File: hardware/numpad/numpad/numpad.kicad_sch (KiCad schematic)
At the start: 33 parts, among them IC1 LD1117-3.3V-SOT223, J1 Conn_01x06, SW2 Push_Button, Y1 8MHz

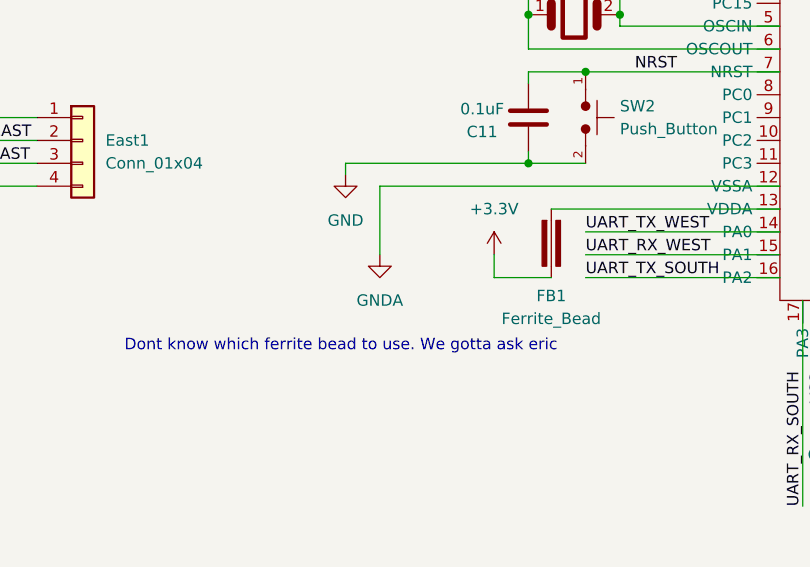
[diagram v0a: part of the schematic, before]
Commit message: typo in schematic
i changed the GNDA to AGND
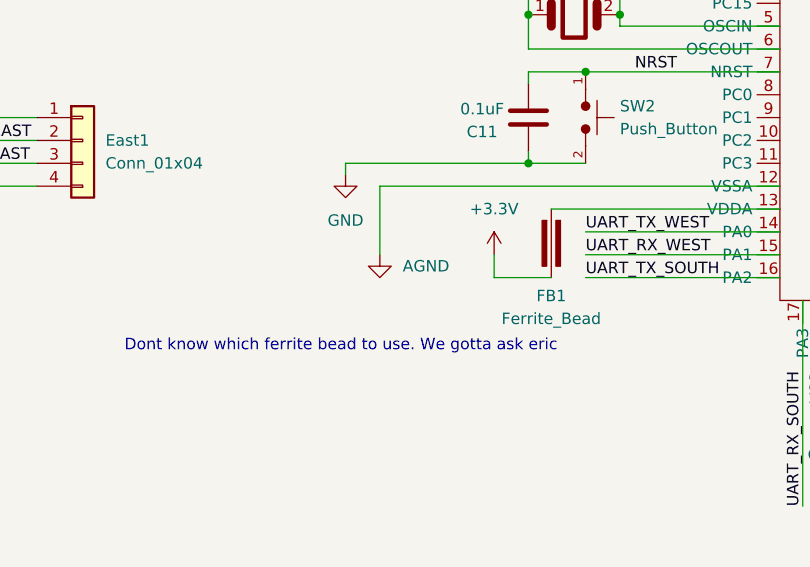
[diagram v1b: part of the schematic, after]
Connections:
- net GNDA renamed AGND
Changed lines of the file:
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@@
 			)
 		)
-		(property "Value" "GNDA"
-			(at 107.95 125.73 0)
+		(property "Value" "AGND"
+			(at 110.49 121.9199 0)
 			(effects
 				(font
 					(size 1.27 1.27)
 				)
+				(justify left)
 			)
 		)

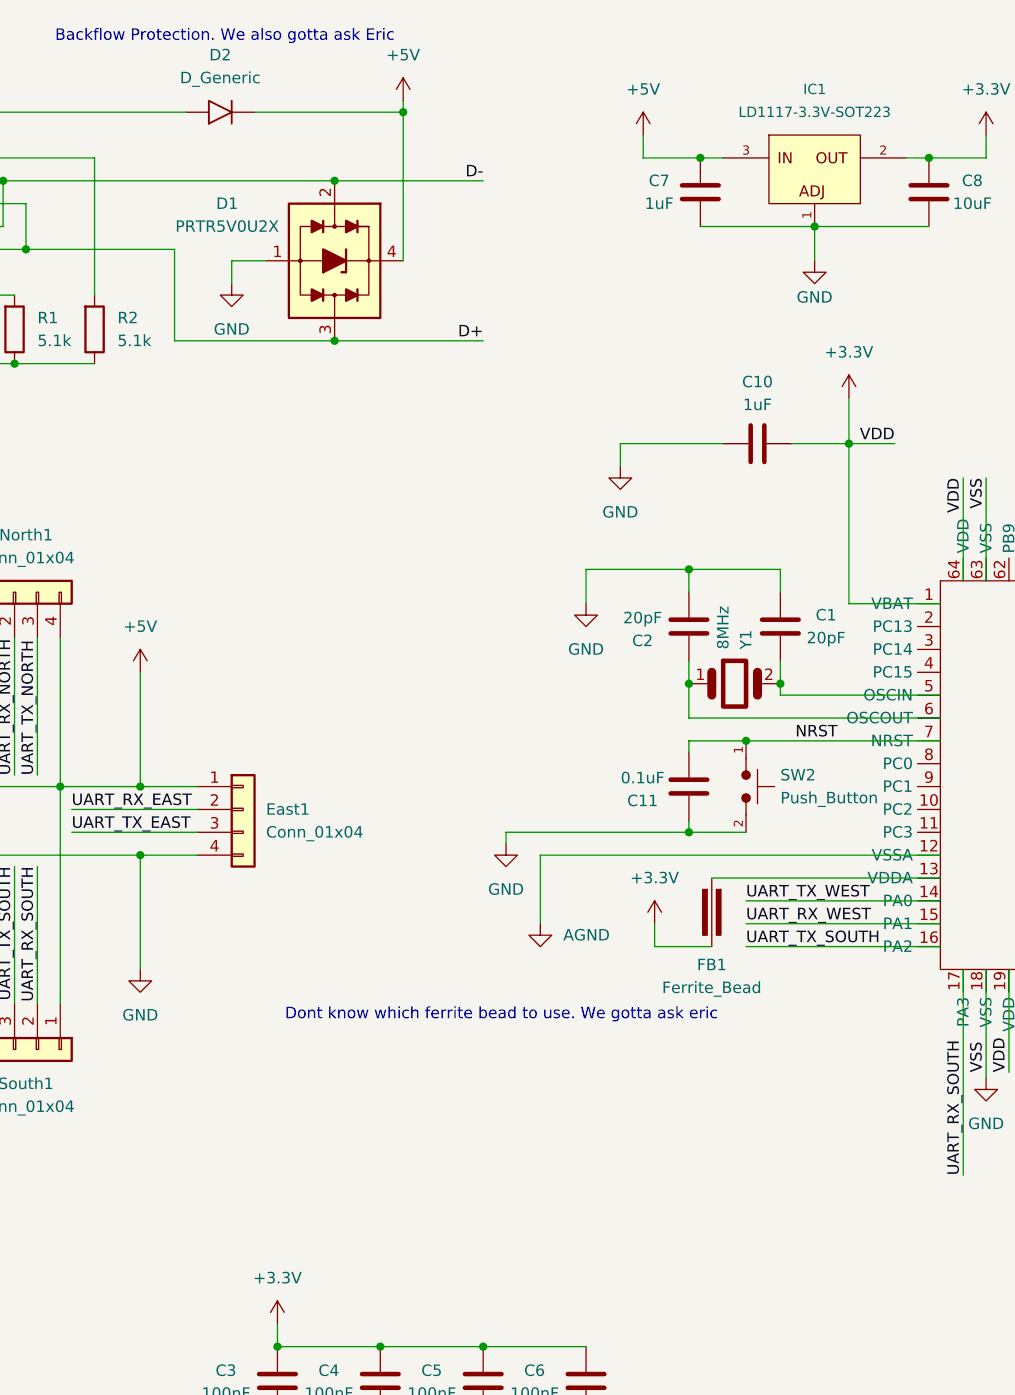
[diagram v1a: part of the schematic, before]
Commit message: diode name + agnd --> gnd
added the bat and added the jump from agnd and gnd that mayyyyy be needed
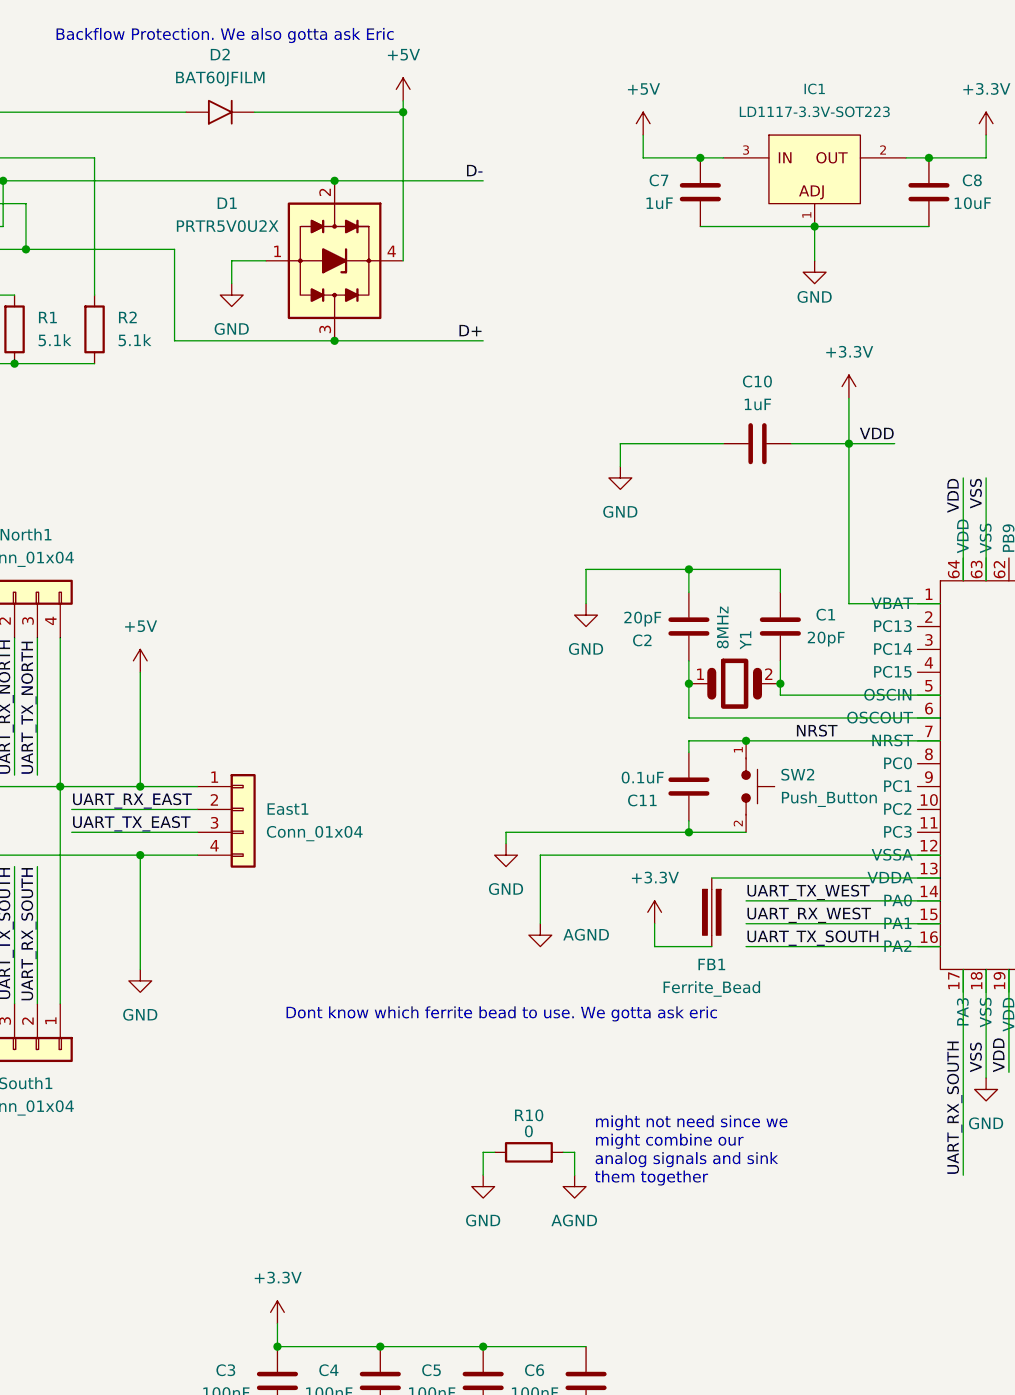
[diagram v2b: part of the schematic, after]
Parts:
- added R10: 0, symbol Device:R
- D2: value D_Generic -> BAT60JFILM
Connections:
- net AGND: now also R10.2
- net GND: now also R10.1

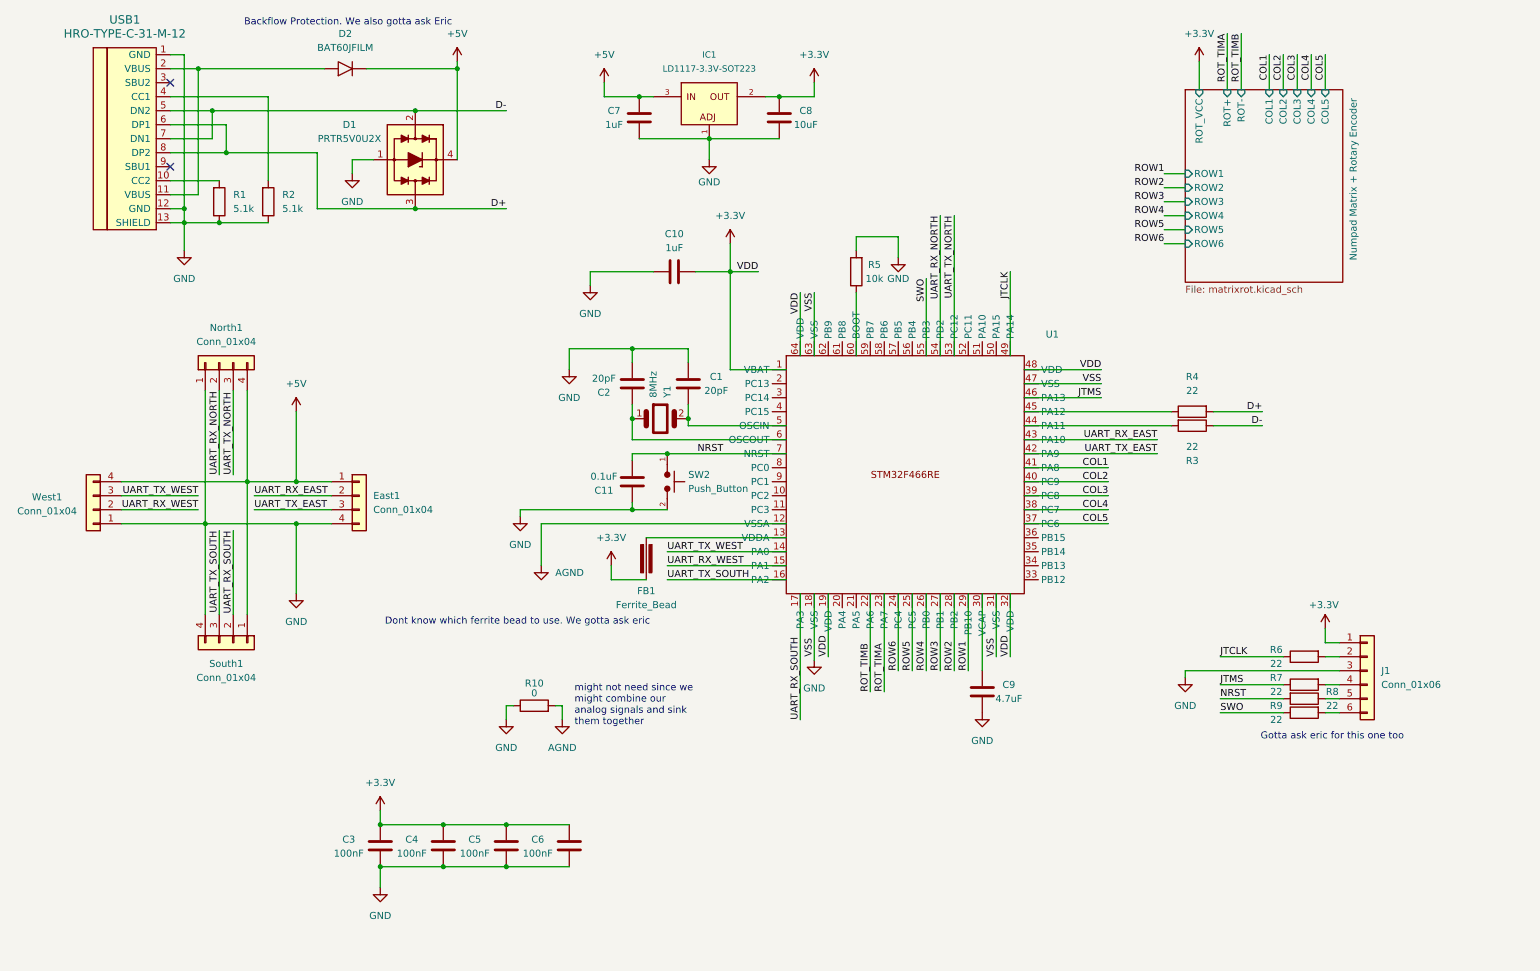
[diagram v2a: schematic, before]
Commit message: rgb matrix and drc rules
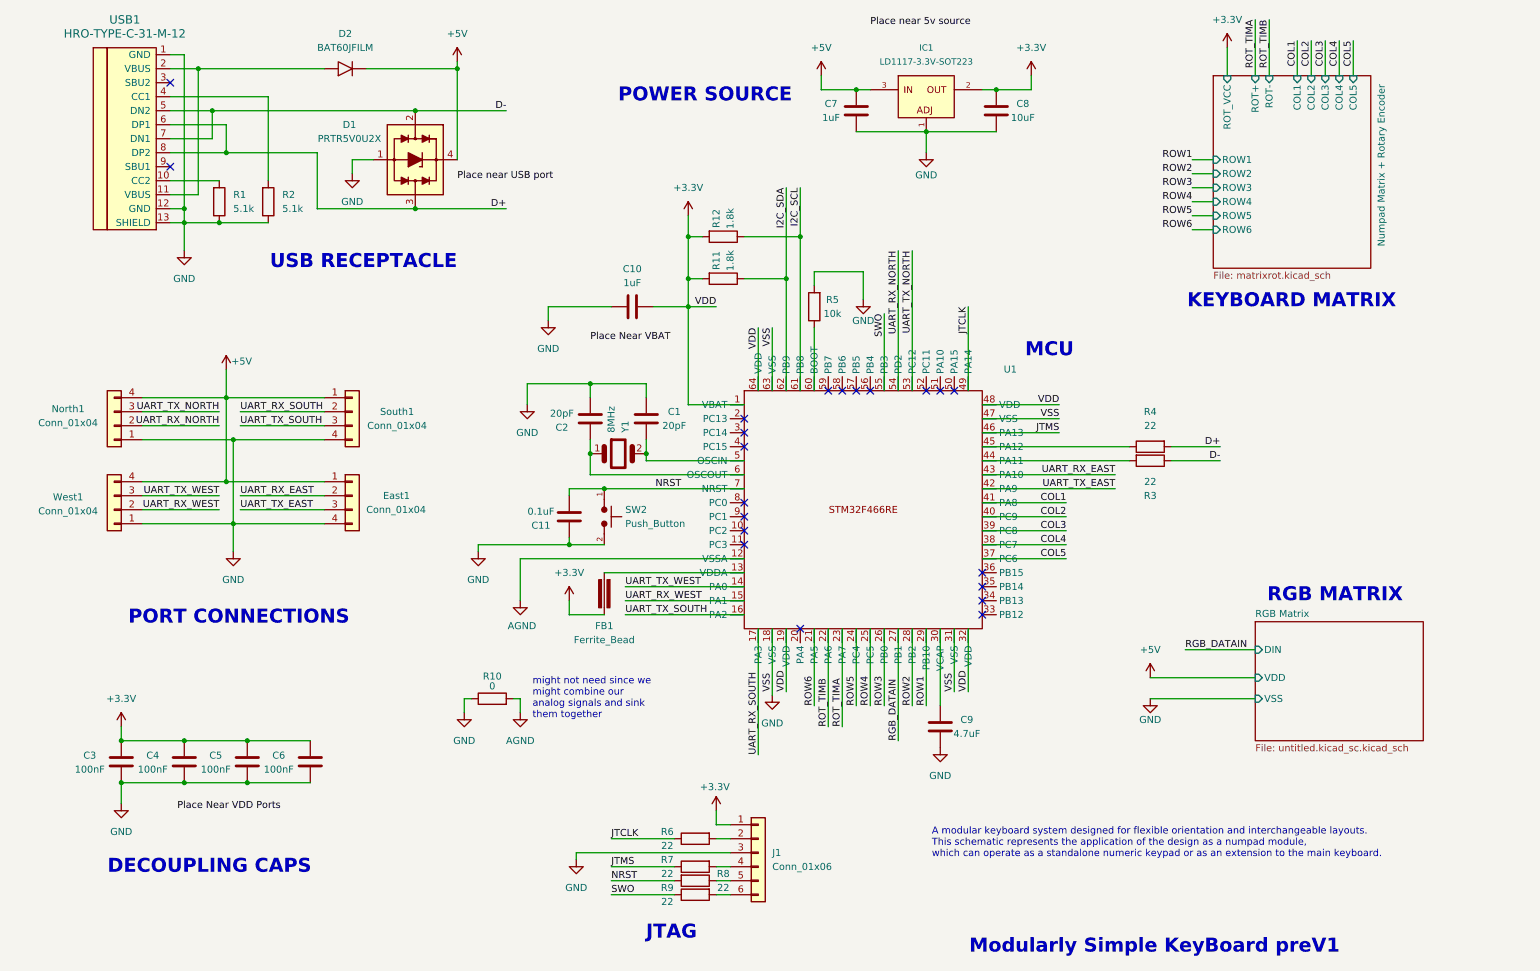
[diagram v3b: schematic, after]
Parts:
- added R11, R12: 1.8k, PCM_Resistor_SMD_AKL:R_0805_2012Metric, symbol PCM_Resistor_AKL:R_0805
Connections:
- net +3.3V: now also R11.1, R12.1
- net ROW3: now also U1.26 (PB0); no longer U1.27 (PB1)
- net ROW4: now also U1.25 (PC5); no longer U1.26 (PB0)
- net ROW5: now also U1.24 (PC4); no longer U1.25 (PC5)
- net ROW6: now also U1.21 (PA5); no longer U1.24 (PC4)
- net I2C_SCL: now reaches U1.61 (PB8)
- net I2C_SCL: now also R12.2
- net I2C_SDA: now reaches U1.62 (PB9)
- net I2C_SDA: now also R11.2
- new net RGB_DATAIN: U1.27 (PB1)
- no-connect marks 2 -> 21
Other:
- added sheet RGB Matrix (untitled.kicad_sc.kicad_sch)
- note added: "A modular keyboard system designed for flexible orientation and interchangeable layouts. This schematic represents the application of the design as a numpad module, which can operate as a standalone numeric keypad or as an extension to the main keyboard."
- note added: "DECOUPLING CAPS"
- note added: "JTAG"
- note added: "KEYBOARD MATRIX"
- note added: "MCU"
- note added: "Modularly Simple KeyBoard preV1"
- note added: "PORT CONNECTIONS"
- note added: "POWER SOURCE"
- note added: "RGB MATRIX"
- note added: "USB RECEPTACLE"
- note removed: "Backflow Protection. We also gotta ask Eric"
- note removed: "Dont know which ferrite bead to use. We gotta ask eric"
- note removed: "Gotta ask eric for this one too"
- moved on the sheet: C1, C10, C11, C2, C3, C4, C5, C6, C7, C8, C9, East1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

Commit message: pcb stuff
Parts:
- removed R10: 0, symbol Device:R
- removed R11, R12: 1.8k, PCM_Resistor_SMD_AKL:R_0805_2012Metric, symbol PCM_Resistor_AKL:R_0805
- added R10, R13: DNP, PCM_Resistor_SMD_AKL:R_0805_2012Metric, symbol PCM_Resistor_AKL:R_0805
- D2: footprint (none) -> PCM_Diode_SMD_AKL:D_SOD-323
- IC1: footprint 4ms_Package_SOT:SOT223 -> PCM_4ms_Package_SOT:SOT223
- J1: footprint 4ms_Connector:Pins_1x06_2.54mm_TH_SWD -> Connector_PinSocket_2.54mm:PinSocket_1x06_P2.54mm_Horizontal
- SW2: footprint Button_Switch_THT:SW_PUSH_6mm -> PCM_marbastlib-various:SW_SPST_SKQG_WithStem
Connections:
- net +3.3V: now also R13.2
- net AGND: now also R10.1
- net GND: now also R10.2
- net NRST: now also R13.1
- net RGB_DATAIN: now also U1.21 (PA5); no longer U1.27 (PB1)
- net ROW3: now also U1.27 (PB1); no longer U1.26 (PB0)
- net ROW4: now also U1.26 (PB0); no longer U1.25 (PC5)
- net ROW5: now also U1.25 (PC5); no longer U1.24 (PC4)
- net ROW6: now also U1.24 (PC4); no longer U1.21 (PA5)
- net UART_RX_EAST: now also U1.14 (PA0); no longer U1.43 (PA10)
- net UART_RX_WEST: now also U1.42 (PA9); no longer U1.15 (PA1)
- net UART_TX_EAST: now also U1.15 (PA1); no longer U1.42 (PA9)
- net UART_TX_WEST: now also U1.43 (PA10); no longer U1.14 (PA0)
- net ROT_SW: now reaches U1.20 (PA4)
- net I2C_SCL: no longer names the net of U1.61 (PB8)
- net I2C_SDA: no longer names the net of U1.62 (PB9)
- no-connect marks 21 -> 22
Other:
- sheet Numpad Matrix + Rotary Encoder renamed NumpadRGB
- removed sheet RGB Matrix
- sheet NumpadRGB ports: added DIN, ROT_SW, VDD, VSS; removed none
- note added: "+ RGB MATRIX"
- note removed: "RGB MATRIX"
- moved on the sheet: J1, R6, R7, R8, R9

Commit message: pcb design draft
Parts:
- D1: footprint PCM_Package_TO_SOT_SMD_AKL:SOT-143 -> PCM_Package_TO_SOT_SMD_AKL:SOT-143_Handsoldering
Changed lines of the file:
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@@
 			)
 		)
-		(property "Footprint" "PCM_Package_TO_SOT_SMD_AKL:SOT-143"
+		(property "Footprint" "PCM_Package_TO_SOT_SMD_AKL:SOT-143_Handsoldering"
 			(at 85.09 46.99 0)
 			(effects
